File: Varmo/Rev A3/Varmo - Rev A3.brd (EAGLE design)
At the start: 136 x 102 mm, 110 parts, among them J1 22-05-7028-02, J2 22-05-7028-02, J3 22-05-7038-03, J4 22-05-7038-03, J5 22-05-7038-03, J6 22-05-7038-03, J7 22-05-7058-05, J9 22-05-7038-03, T1 MMBT2222AL, U1 LT1813, U2 SN74LVC2G17DBVR, U3 SN74LVC2G17DBVR, U4 PCA9665D, U5 90814-0210, U6 90814-0210, U8 M20DX256, X1 90814-0210, X2 90814-0210, X6 NC5MAV-SW, X7 90814-0210, X8 90814-0210

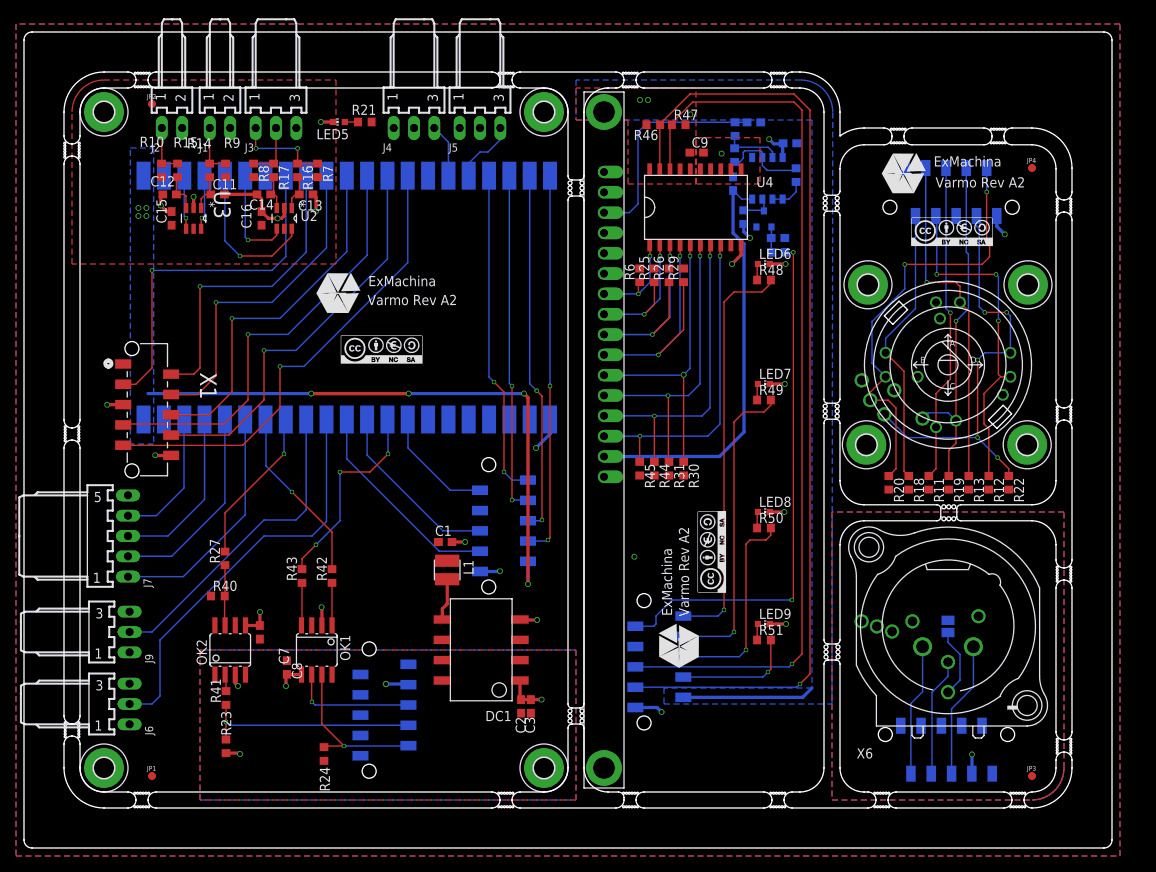
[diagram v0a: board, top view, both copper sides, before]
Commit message: Fix #7 : Replace M2.5 drill by M3
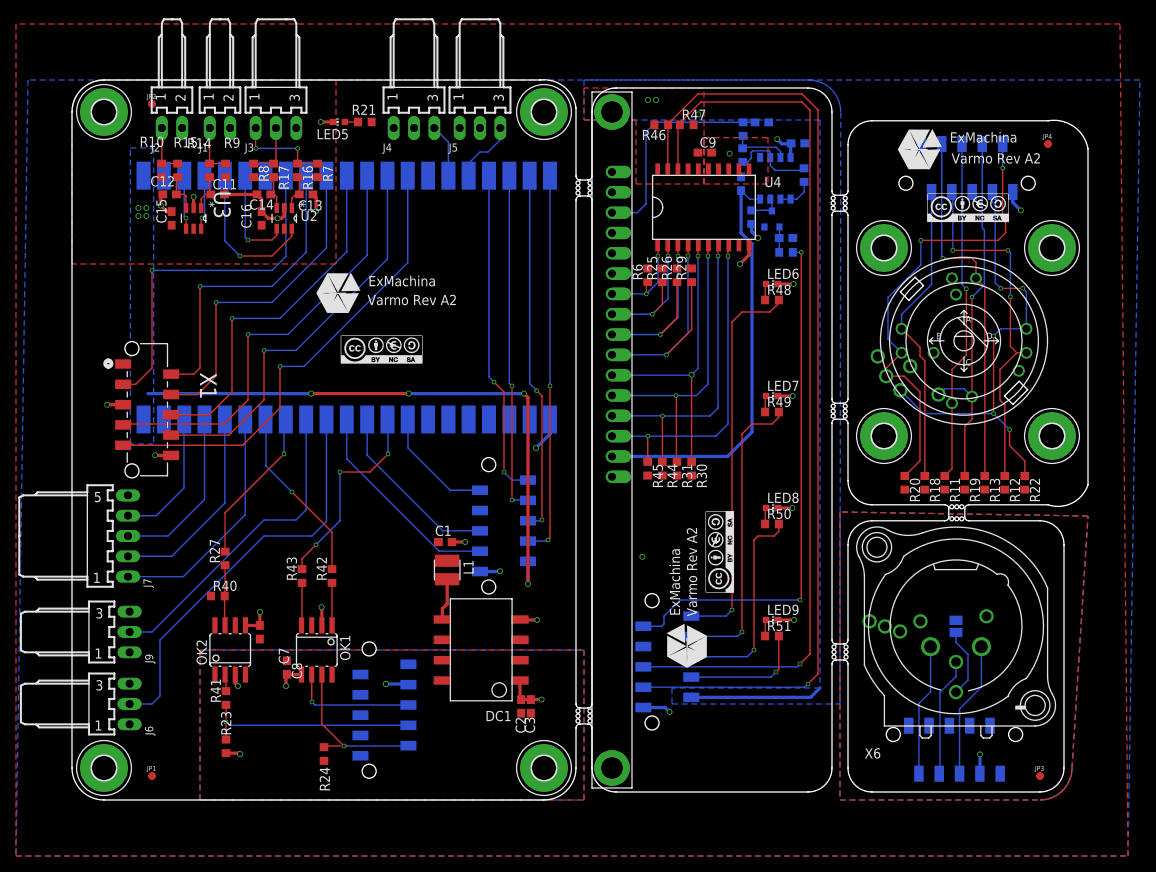
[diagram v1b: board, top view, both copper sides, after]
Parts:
- MP1, MP2, MP3, MP4, MP5, MP6, MP7, MP8: value MOUNT-PAD2.5 -> MOUNT-PAD3,0; device holes:P2.5 -> holes:P3,0
- moved MP5 29.8 mm to (121.5, 44.5)
- moved MP6 24.7 mm to (100.5, 68.0)
- moved MP7 17.9 mm to (100.5, 44.5)
- moved MP8 5.49 mm to (121.5, 68.0)
- moved ENC1 3.61 mm to (110.5, 56.4)
- moved JP4 3.61 mm to (121.0, 81.0)
- moved U$2 3.61 mm to (110.5, 56.4)
- moved U$3 3.61 mm to (104.9, 80.3)
- moved U$4 3.61 mm to (111.0, 73.0)
- moved X2 3.61 mm to (116.6, 75.0)
- moved LED6 2.69 mm to (86.5, 63.5)
- moved R48 2.69 mm to (86.5, 61.5)
- moved R11 2.00 mm to (108.1, 38.6)
- moved R12 2.00 mm to (115.6, 38.6)
- moved R13 2.00 mm to (113.1, 38.6)
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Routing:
- net ENCODER_A: track 93.6 -> 97.5 mm
- net PUSH: track 85.9 -> 88.9 mm
- net DIR_D: track 94.2 -> 97.2 mm
- net DIR_C: track 93.1 -> 96.1 mm
- net DIR_A: track 85.1 -> 88.1 mm
- net ENCODER_B: track 98.2 -> 101.2 mm
- net DIR_B: track 96.6 -> 99.4 mm
- net LED_STATUS_1: track 92.4 -> 89.9 mm
- net LED_STATUS_2: track 81.6 -> 80.1 mm
- net LED_STATUS_4: track 63.2 -> 63.7 mm
- net LED_STATUS_3: track 71.4 -> 71.9 mm
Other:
- board size 136 x 102 mm -> 127 x 90 mm

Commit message: REplace the old version of LCD Screen by the new one
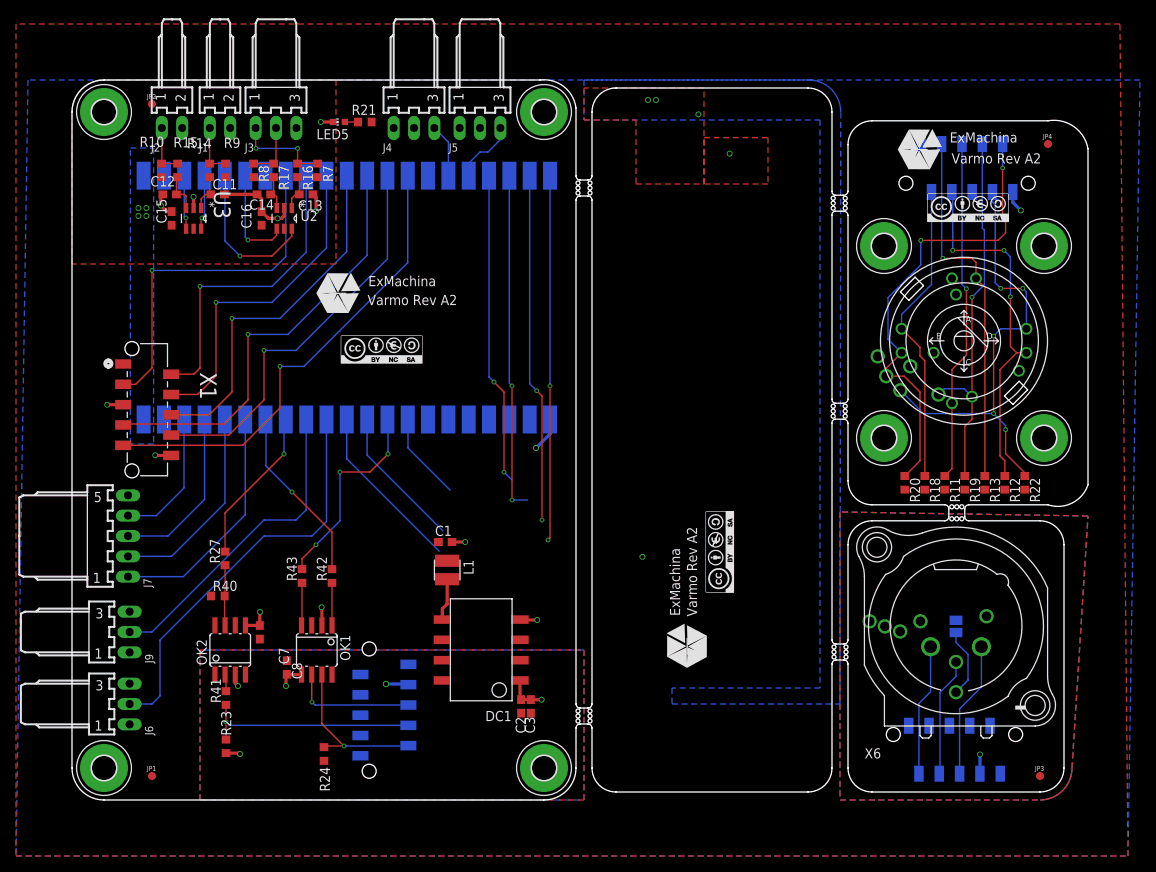
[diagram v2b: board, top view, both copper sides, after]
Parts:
- removed C10, C4, C6, C9: 0.1uF, rcl:C0603
- removed C5: 4.7uF, rcl:C0603
- removed LCD1: MC41605A12W, midas:CONNECTOR
- removed LED6, LED7, LED8, LED9: Blue, led:CHIP-LED0603
- removed R1: 100R, rcl:R0603
- removed R2, R3, R4, R48, R49, R50, R51: 1k, rcl:R0603
- removed R25, R26, R29, R30, R31, R44, R45, R46, R47, R6: 4.7k, rcl:R0603
- removed R5: 10k, rcl:R0603
- removed T1: MMBT2222AL, transistor:SOT−23
- removed U1: LT1813, lineartechnology:S8
- removed U4: PCA9665D, NXP:SOT163-1
- removed U5, U6: 90814-0210, Molex_By_element14_Batch_1:MOLEX_90814-0210
- moved MP5 1.03 mm to (120.5, 44.2)
- moved MP8 1.03 mm to (120.5, 68.2)
- moved MP6 0.25 mm to (100.5, 68.2)
- moved MP7 0.25 mm to (100.5, 44.2)
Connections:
- removed net D0: LCD1.7, R6.1, U4.1
- removed net D1: LCD1.8, R25.1, U4.2
- removed net D2: LCD1.9, R26.1, U4.3
- removed net D3: LCD1.10, R29.1, U4.4
- removed net D4: LCD1.11, R30.1, U4.5
- removed net D5: LCD1.12, R31.1, U4.6
- removed net D6: LCD1.13, R44.1, U4.7
- removed net D7: LCD1.14, R45.1, U4.8
- removed net N$14: R3.1, R4.2, U1.6
- removed net N$17: R4.1, R5.2, U1.7
- removed net N$2: C4.1, R1.2, T1.1
- removed net N$22: LED7.A, R49.1
- removed net N$24: LED8.A, R50.1
- removed net N$29: LED9.A, R51.1
- removed net N$3: R2.1, T1.3, U1.3
- removed net N$4: LED6.A, R48.1
- removed net N$5: R3.2, U1.1, U1.2
- removed net VEE: C10.1, LCD1.15, U1.4
- removed net VO: C5.1, LCD1.3, R5.1
- net +3V3: no longer C9.1, R46.2, R47.2, U4.20, U5.2, U6.2
- net +5V/1: no longer C6.1, LCD1.2, LCD1.4, LCD1.6, R2.2, R25.2, R26.2, R29.2, R30.2, R31.2, R44.2, R45.2, R6.2, U1.8, U5.1, U6.1
- net GND1: no longer C10.2, C4.2, C5.2, C6.2, C9.2, LCD1.1, LCD1.16, LCD1.5, LED6.C, LED7.C, LED8.C, LED9.C, T1.2, U1.5, U4.10, U4.11, U4.12, U4.13, U4.14, U4.15, U5.7, U6.7
- net LED_STATUS_1: no longer R48.2, U5.10, U6.10
- net LED_STATUS_2: no longer R49.2, U5.8, U6.8
- net LED_STATUS_3: no longer R50.2, U5.6, U6.6
- net LED_STATUS_4: no longer R51.2, U5.4, U6.4
- net PWM_CONTRASTE: no longer R1.1, U5.9, U6.9
- net SCL: no longer R47.1, U4.18, U5.5, U6.5
- net SDA: no longer R46.1, U4.19, U5.3, U6.3
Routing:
- net SDA: track 146.2 -> 21.2 mm, vias 1 -> 0
- net SCL: track 135.7 -> 17.8 mm, vias 1 -> 0
- net +3V3: track 90.4 -> 0.00 mm, vias 11 -> 7
- net PWM_CONTRASTE: track 80.9 -> 11.0 mm, vias 2 -> 0
- net VEE: track 52.4 -> 0.00 mm
- net LED_STATUS_1: track 89.9 -> 39.2 mm, vias 3 -> 2
- net D7: track 40.7 -> 0.00 mm, vias 2 -> 0
- net D6: track 39.8 -> 0.00 mm, vias 2 -> 0
- net D5: track 38.3 -> 0.00 mm, vias 2 -> 0
- net LED_STATUS_2: track 80.1 -> 42.6 mm, vias 3 -> 2
- net D4: track 37.4 -> 0.00 mm, vias 2 -> 0
- net D3: track 32.0 -> 0.00 mm, vias 2 -> 0
- net LED_STATUS_3: track 71.9 -> 43.8 mm, vias 3 -> 2
- net VO: track 27.9 -> 0.00 mm
- net D2: track 25.5 -> 0.00 mm, vias 2 -> 0
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
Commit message: Replace LED postiiton
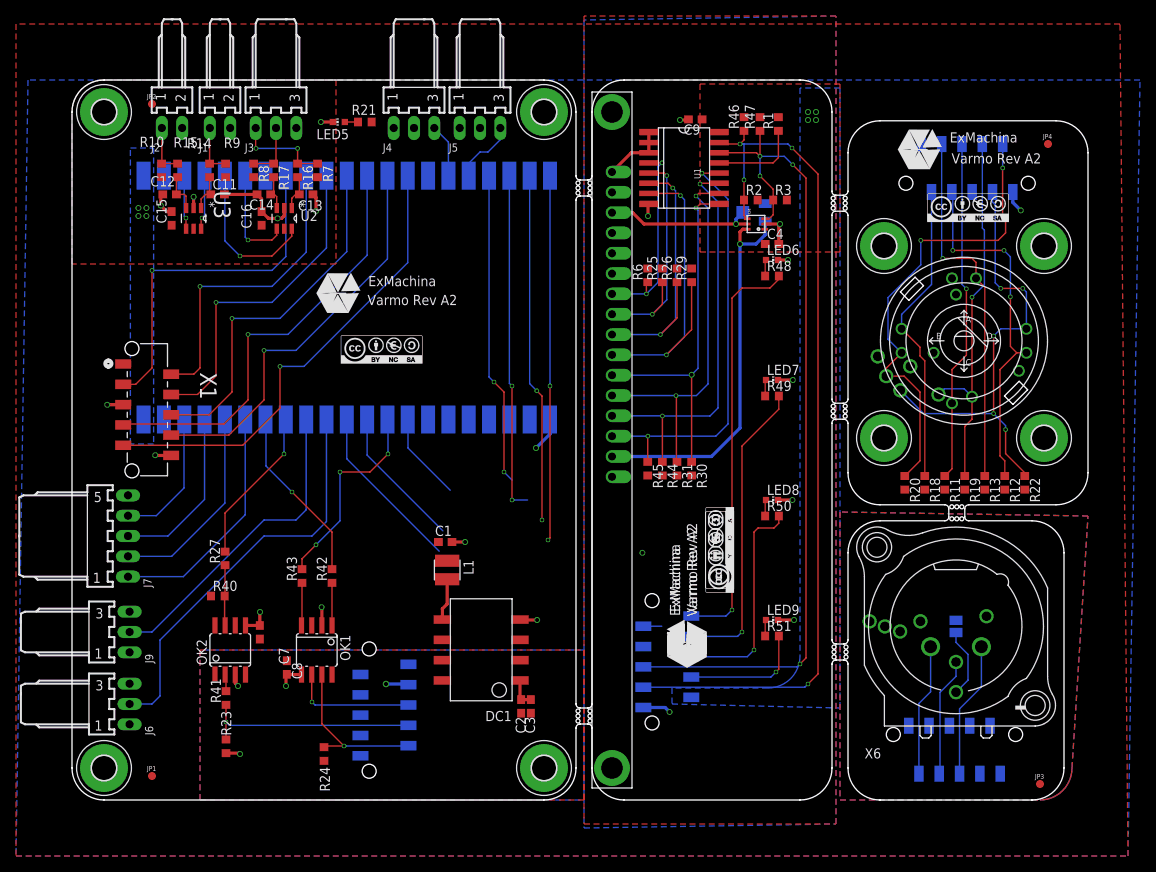
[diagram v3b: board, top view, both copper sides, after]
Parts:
- added C4, C9: 0.1uF, rcl:C0603
- added LCD1: MC41605A12W, midas:CONNECTOR
- added LED6, LED7, LED8, LED9: Blue, led:CHIP-LED0603
- added R1, R2, R25, R26, R29, R3, R30, R31, R44, R45, R46, R47, R6: 4.7k, rcl:R0603
- added R4: 3313J-1-103E, pot:3313J
- added R48, R49, R50, R51: 1k, rcl:R0603
- added U$8: CC-BY-NC-SA, cc-by-sa:CC-BY-NC-SA
- added U$9: EXMACHINA-LOGO-NAME, exmachina:EXM-LOGO-BASELINE
- added U1: PCA9670D, NXP:SOT162-1
- added U4: TPL0401A, ti:SC-70-DCK
- added U5: 90814-0210, Molex_By_element14_Batch_1:MOLEX_90814-0210
- moved JP3 1.00 mm to (120.0, 1.00)
- moved U$5 0.50 mm to (80.0, 30.5)
- moved U$7 0.50 mm to (75.9, 18.7)
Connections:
- new net +3V1: C4.1, C9.1, R1.2, R2.2, R3.2, R46.2, R47.2, U1.16, U4.1, U5.2
- new net +5V/2: LCD1.2, LCD1.4, LCD1.6, R25.2, R26.2, R29.2, R30.2, R31.2, R44.2, R45.2, R6.2, U5.1
- new net D0: LCD1.7, R6.1, U1.4
- new net D1: LCD1.8, R25.1, U1.5
- new net D2: LCD1.9, R26.1, U1.6
- new net D3: LCD1.10, R29.1, U1.7
- new net D4: LCD1.11, R30.1, U1.9
- new net D5: LCD1.12, R31.1, U1.10
- new net D6: LCD1.13, R44.1, U1.11
- new net D7: LCD1.14, R45.1, U1.12
- new net GND2: C4.2, C9.2, LCD1.1, LCD1.16, LCD1.5, LED6.C, LED7.C, LED8.C, LED9.C, R4.3, U1.1, U1.2, U1.3, U1.8, U4.2, U5.7
- new net LED_STATUS_5: R49.2, U5.8
- new net LED_STATUS_6: R50.2, U5.6
- new net LED_STATUS_7: R51.2, U5.4
- new net LED_STATUS_8: R48.2, U5.10
- new net N$2: R1.1, U1.13
- new net N$22: LED7.A, R49.1
- new net N$24: LED8.A, R50.1
- new net N$29: LED9.A, R51.1
- new net N$4: LED6.A, R48.1
- new net PWM_CONTRASTE1: U5.9
- new net S$1: U8.12, X1.4
- new net SCL1: R3.1, R47.1, U1.14, U4.3, U5.5
- new net SDA1: R2.1, R46.1, U1.15, U4.4, U5.3
- new net VEE: LCD1.15, R4.1, U4.6
- new net VO: LCD1.3, R4.2, U4.5
- net PUSH: no longer U8.12, X1.4
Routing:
- net SDA1: track 0.00 -> 110.4 mm, vias 0 -> 4
- net SCL1: track 0.00 -> 105.4 mm, vias 0 -> 4
- net D7: track 0.00 -> 53.2 mm, vias 0 -> 2
- net LED_STATUS_8: track 0.00 -> 51.6 mm, vias 0 -> 1
- net D6: track 0.00 -> 50.8 mm, vias 0 -> 2
- net VEE: track 0.00 -> 48.3 mm, vias 0 -> 1
- net D5: track 0.00 -> 48.1 mm, vias 0 -> 2
- net D4: track 0.00 -> 45.3 mm, vias 0 -> 2
- net D3: track 0.00 -> 42.3 mm, vias 0 -> 2
- net S$1: track 0.00 -> 41.4 mm, vias 0 -> 1
- net PUSH: track 88.9 -> 47.5 mm, vias 2 -> 1
- net LED_STATUS_5: track 0.00 -> 38.0 mm, vias 0 -> 1
- net D2: track 0.00 -> 36.0 mm, vias 0 -> 2
- net D1: track 0.00 -> 30.0 mm, vias 0 -> 2
- net LED_STATUS_6: track 0.00 -> 27.4 mm, vias 0 -> 1
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- added copper zone on layer 1, net +3V1
- added copper zone on layer 16, net +3V1
- added copper zone on layer 1, net +5V/2
- added copper zone on layer 16, net GND2
- removed copper zone on layer 1, net GND1
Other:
- outline, holes or cut-outs redrawn

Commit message: Fix #9 : Change PCA9670D to PCA9671D and route the LCD Board
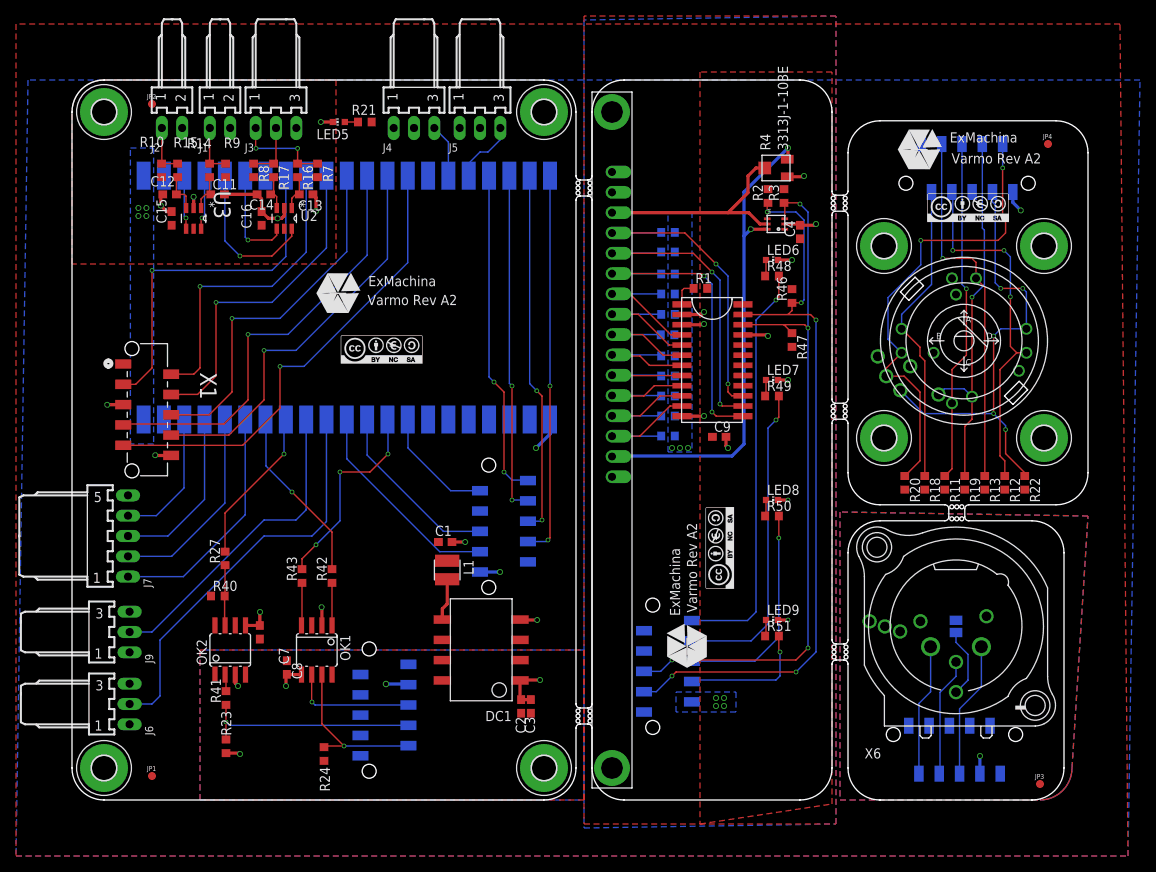
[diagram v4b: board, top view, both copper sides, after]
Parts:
- removed U$7: EXMACHINA-LOGO-NAME, exmachina:EXM-LOGO-BASELINE
- removed U$8: CC-BY-NC-SA, cc-by-sa:CC-BY-NC-SA
- added R28, R32, R5: 4.7k, rcl:R0603
- added U$10: PCA9671D, NXP:SOT137-1
- U$2: value EC20AE -> EC20A1824401
- U1: value PCA9670D -> 90814-0210; device NXP:SOT162-1 -> Molex_By_element14_Batch_1:MOLEX_90814-0210
- moved U1 56.6 mm to (50.0, 27.5), flipped to the bottom, turned to 90 degrees
- moved C9 39.8 mm to (79.9, 44.4), turned to 0 degrees
- moved R47 27.3 mm to (89.0, 56.5), turned to 270 degrees
- moved R1 22.7 mm to (77.5, 63.0), turned to 0 degrees
- moved R46 22.3 mm to (89.0, 62.0)
- moved R30 12.0 mm to (73.5, 52.0), flipped to the bottom, turned to 180 degrees
- moved R29 10.5 mm to (73.5, 54.5), flipped to the bottom, turned to 180 degrees
- moved R31 9.16 mm to (73.5, 49.5), flipped to the bottom, turned to 180 degrees
- moved R26 7.53 mm to (73.5, 57.1), flipped to the bottom, turned to 180 degrees
- moved R44 6.63 mm to (73.5, 47.0), flipped to the bottom, turned to 180 degrees
- moved R4 6.19 mm to (87.0, 78.0), flipped to the top, turned to 90 degrees
- moved R25 4.94 mm to (73.5, 59.7), flipped to the bottom, turned to 180 degrees
- moved R45 4.81 mm to (73.5, 44.5), flipped to the bottom, turned to 180 degrees
- moved C4 3.81 mm to (90.0, 70.0), turned to 90 degrees
- moved R6 3.45 mm to (73.5, 62.2), flipped to the bottom, turned to 180 degrees
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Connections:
- removed net +3V1: C4.1, C9.1, R1.2, R2.2, R3.2, R46.2, R47.2, U1.16, U4.1, U5.2
- removed net +5V/2: LCD1.2, LCD1.4, LCD1.6, R25.2, R26.2, R29.2, R30.2, R31.2, R44.2, R45.2, R6.2, U5.1
- removed net GND2: C4.2, C9.2, LCD1.1, LCD1.16, LCD1.5, LED6.C, LED7.C, LED8.C, LED9.C, R4.3, U1.1, U1.2, U1.3, U1.8, U4.2, U5.7
- removed net LED_STATUS_5: R49.2, U5.8
- removed net LED_STATUS_6: R50.2, U5.6
- removed net LED_STATUS_7: R51.2, U5.4
- removed net LED_STATUS_8: R48.2, U5.10
- removed net PWM_CONTRASTE1: U5.9
- removed net S$1: U8.12, X1.4
- removed net SCL1: R3.1, R47.1, U1.14, U4.3, U5.5
- removed net SDA1: R2.1, R46.1, U1.15, U4.4, U5.3
- new net E: LCD1.6, R5.1, U$10.13
- new net R/W: LCD1.5, R28.1, U$10.14
- new net RS: LCD1.4, R32.1, U$10.15
- net +3V3: now also C4.1, C9.1, R1.2, R2.2, R3.2, R46.2, R47.2, U$10.24, U1.2, U4.1, U5.2
- net +5V/1: now also LCD1.2, R25.2, R26.2, R28.2, R29.2, R30.2, R31.2, R32.2, R44.2, R45.2, R5.2, R6.2, U1.1, U5.1
- net D0: now also U$10.4; no longer U1.4
- net D1: now also U$10.5; no longer U1.5
- net D2: now also U$10.6; no longer U1.6
- net D3: now also U$10.7; no longer U1.7
- net D4: now also U$10.8; no longer U1.9
- net D5: now also U$10.9; no longer U1.10
- net D6: now also U$10.10; no longer U1.11
- net D7: now also U$10.11; no longer U1.12
- net GND1: now also C4.2, C9.2, LCD1.1, LCD1.16, LED6.C, LED7.C, LED8.C, LED9.C, R4.3, U$10.12, U$10.2, U$10.21, U$10.3, U1.7, U4.2, U5.7
- net LED_STATUS_1: now also R48.2, U1.10, U5.10
- net LED_STATUS_2: now also R49.2, U1.8, U5.8
- net LED_STATUS_3: now also R50.2, U1.6, U5.6
- net LED_STATUS_4: now also R51.2, U1.4, U5.4
- net N$2: now also U$10.1; no longer U1.13
- net PUSH: now also U8.12, X1.4
- net PWM_CONTRASTE: now also U1.9; no longer U8.35
- net SCL: now also R3.1, R47.1, U$10.22, U1.5, U4.3, U5.5
- net SDA: now also R2.1, R46.1, U$10.23, U1.3, U4.4, U5.3
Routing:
- net SDA1: track 110.4 -> 0.00 mm, vias 4 -> 0
- net SCL1: track 105.4 -> 0.00 mm, vias 4 -> 0
- net SDA: track 21.2 -> 121.2 mm, vias 0 -> 5
- net SCL: track 17.8 -> 114.0 mm, vias 0 -> 4
- net LED_STATUS_1: track 39.2 -> 92.9 mm, vias 2 -> 3
- net LED_STATUS_8: track 51.6 -> 0.00 mm, vias 1 -> 0
- net PUSH: track 47.5 -> 88.9 mm, vias 1 -> 2
- net S$1: track 41.4 -> 0.00 mm, vias 1 -> 0
- net R/W: track 0.00 -> 39.6 mm, vias 0 -> 2
- net RS: track 0.00 -> 39.5 mm, vias 0 -> 2
- net LED_STATUS_2: track 42.6 -> 82.1 mm, vias 2 -> 3
- net E: track 0.00 -> 39.3 mm, vias 0 -> 2
- net LED_STATUS_5: track 38.0 -> 0.00 mm, vias 1 -> 0
- net D7: track 53.2 -> 16.5 mm, vias 2 -> 0
- net D6: track 50.8 -> 15.9 mm, vias 2 -> 0
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- added copper zone on layer 16, net +5V/1
- removed copper zone on layer 1, net +3V1
- removed copper zone on layer 16, net +3V1
- removed copper zone on layer 1, net +5V/2
- removed copper zone on layer 16, net GND2
